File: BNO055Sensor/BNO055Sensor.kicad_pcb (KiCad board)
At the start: 4 copper layers, 50 x 35 mm, 3 parts, among them J1 locked

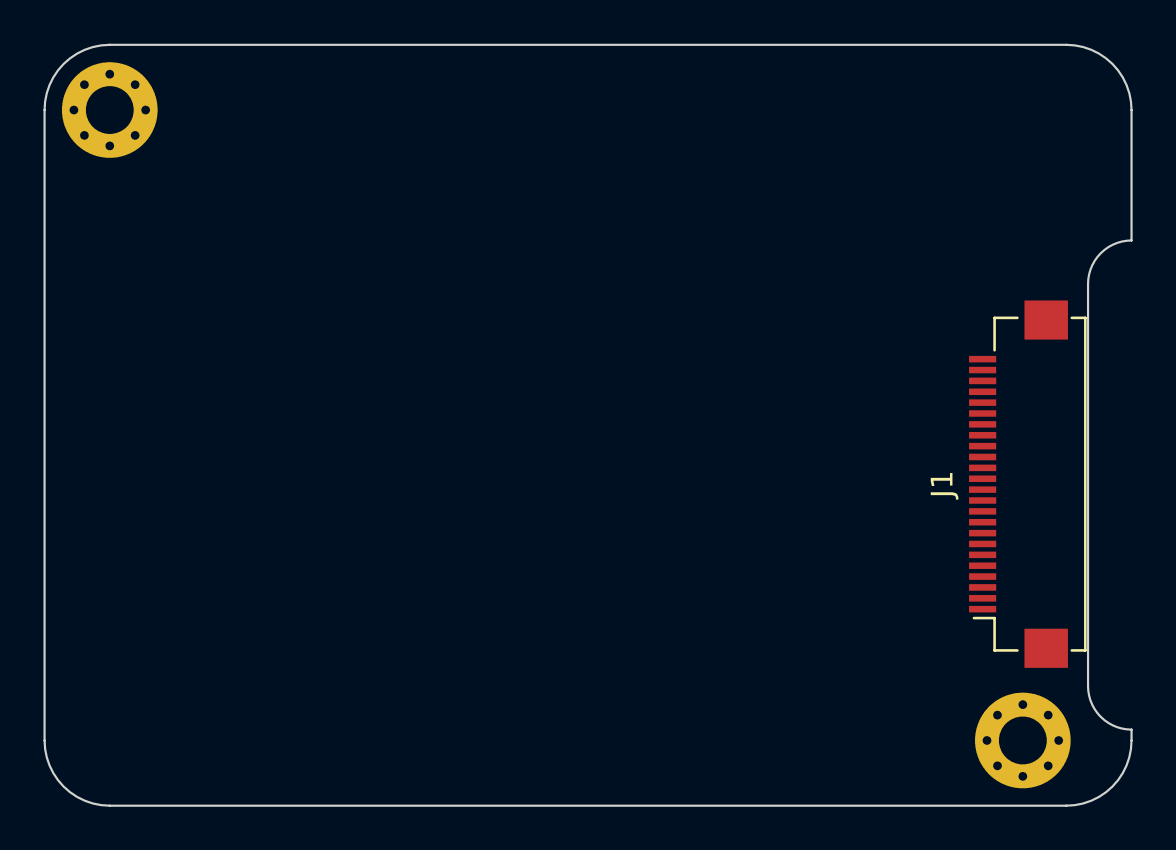
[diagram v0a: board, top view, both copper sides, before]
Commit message: Roughly places components on BNO055 sensor pcb
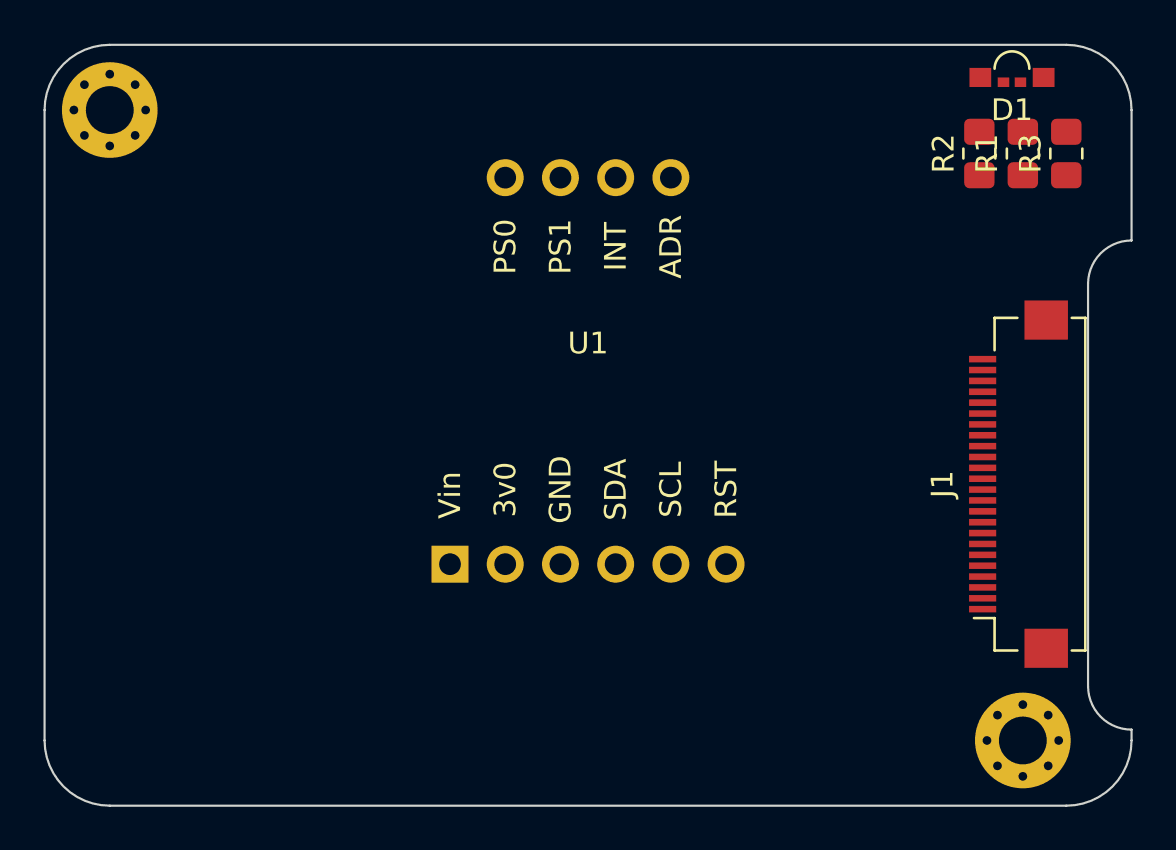
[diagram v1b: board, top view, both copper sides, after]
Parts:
- added D1: LED_RGBA, GameOver:Hongzhi_Forest_HS-1204-RGB, F.Cu at (164.5, 81.5)
- added R1: 1kΩ, Resistor_SMD:R_0805_2012Metric_Pad1.20x1.40mm_HandSolder, F.Cu at (165.0, 85.0)
- added R2: 1kΩ, Resistor_SMD:R_0805_2012Metric_Pad1.20x1.40mm_HandSolder, F.Cu at (163.0, 85.0)
- added R3: 1kΩ, Resistor_SMD:R_0805_2012Metric_Pad1.20x1.40mm_HandSolder, F.Cu at (167.0, 85.0)
- added U1: Adafruit_BNO055_breakout, GameOver:Adafruit_BNO055_breakout, F.Cu at (145.0, 93.7)
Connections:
- net 3v3 renamed +3V3
- H1 pad 1: unconnected-(H1-Pad1) -> GND
- H2 pad 1: unconnected-(H2-Pad1) -> GND
- J1 pad 10: unconnected-(J1-IO5) -> PS0
- J1 pad 11: unconnected-(J1-IO17) -> PS1
- J1 pad 14: unconnected-(J1-IO16) -> INT
- J1 pad 15: unconnected-(J1-IO4) -> ADR
- J1 pad 20: unconnected-(J1-IO35) -> LED_B
- J1 pad 21: unconnected-(J1-IO32) -> LED_G
- J1 pad 22: unconnected-(J1-IO33) -> LED_R
- J1 pad 5: unconnected-(J1-IO21) -> RST
- J1 pad 6: unconnected-(J1-IO19) -> SDA
- J1 pad 9: unconnected-(J1-IO18) -> SCL

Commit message: Adds copper pours for gnd and 3v3 on sensor board
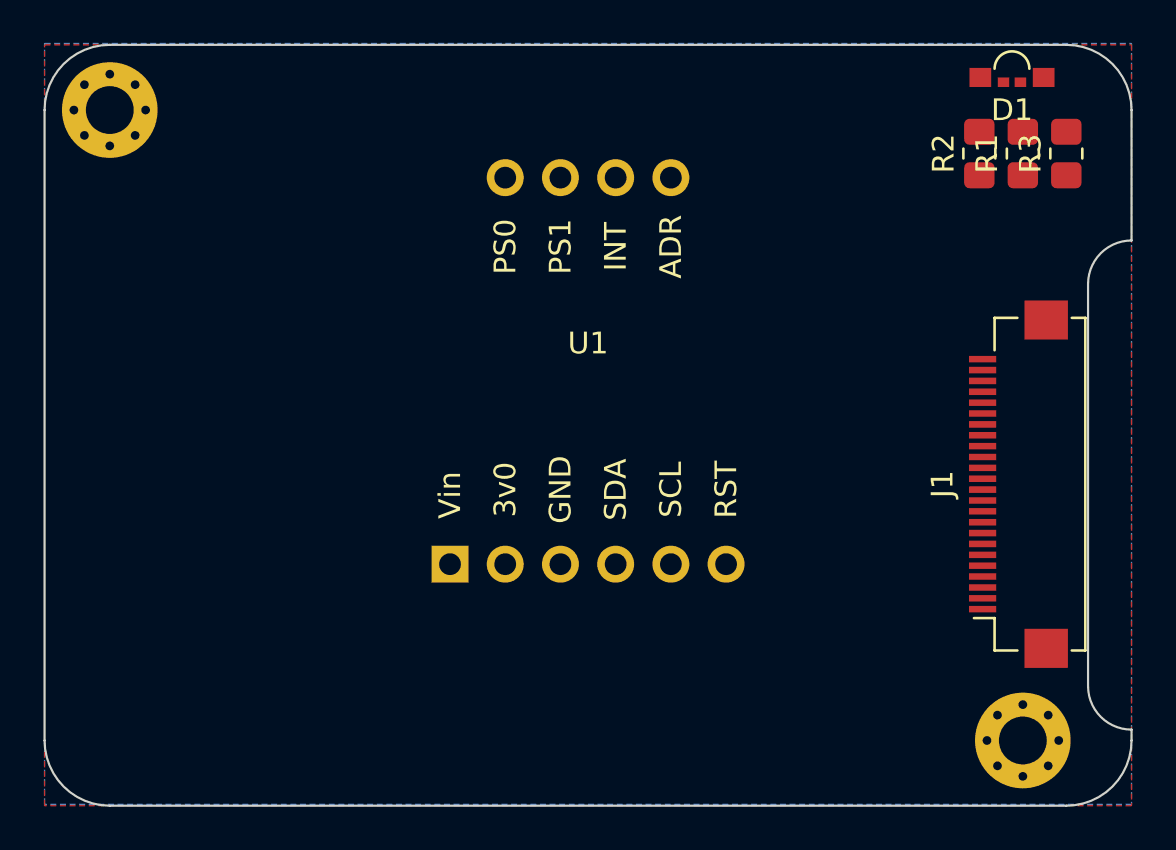
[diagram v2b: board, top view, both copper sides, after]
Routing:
- added copper zone on F.Cu, net +3V3
- added copper zone on B.Cu, net GND
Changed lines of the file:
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@@
   (gr_arc locked (start 167 80) (mid 169.12132 80.87868) (end 170 83)
     (stroke (width 0.1) (type default)) (layer "Edge.Cuts"))
+  (zone (net 7) (net_name "+3V3") (layer "F.Cu") (hatch edge 0.508)
+    (connect_pads (clearance 0.508))
+    (min_thickness 0.254) (filled_areas_thickness no)
+    (fill yes (thermal_gap 0.508) (thermal_bridge_width 0.508) (island_removal_mode 2) (island_area_min 10))
+    (polygon
+      (pts
+        (xy 170 115)
+        (xy 120 115)
+        (xy 120 80)
+        (xy 170 80)
+      )
+    )
+  )
+  (zone (net 1) (net_name "GND") (layer "B.Cu") (hatch edge 0.508)
+    (connect_pads (clearance 0.508))
+    (min_thickness 0.254) (filled_areas_thickness no)
+    (fill yes (thermal_gap 0.508) (thermal_bridge_width 0.508) (island_removal_mode 2) (island_area_min 10))
+    (polygon
+      (pts
+        (xy 170 114.93809)
+        (xy 120 114.93809)
+        (xy 120 79.93809)
+        (xy 170 79.93809)
+      )
+    )
+  )
 )

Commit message: Routes BNO055 breakout board
The SDA/SCL pins shouldn't be swapped as we're using the hardware i2c
which are in set pins on the esp32 (18/19).
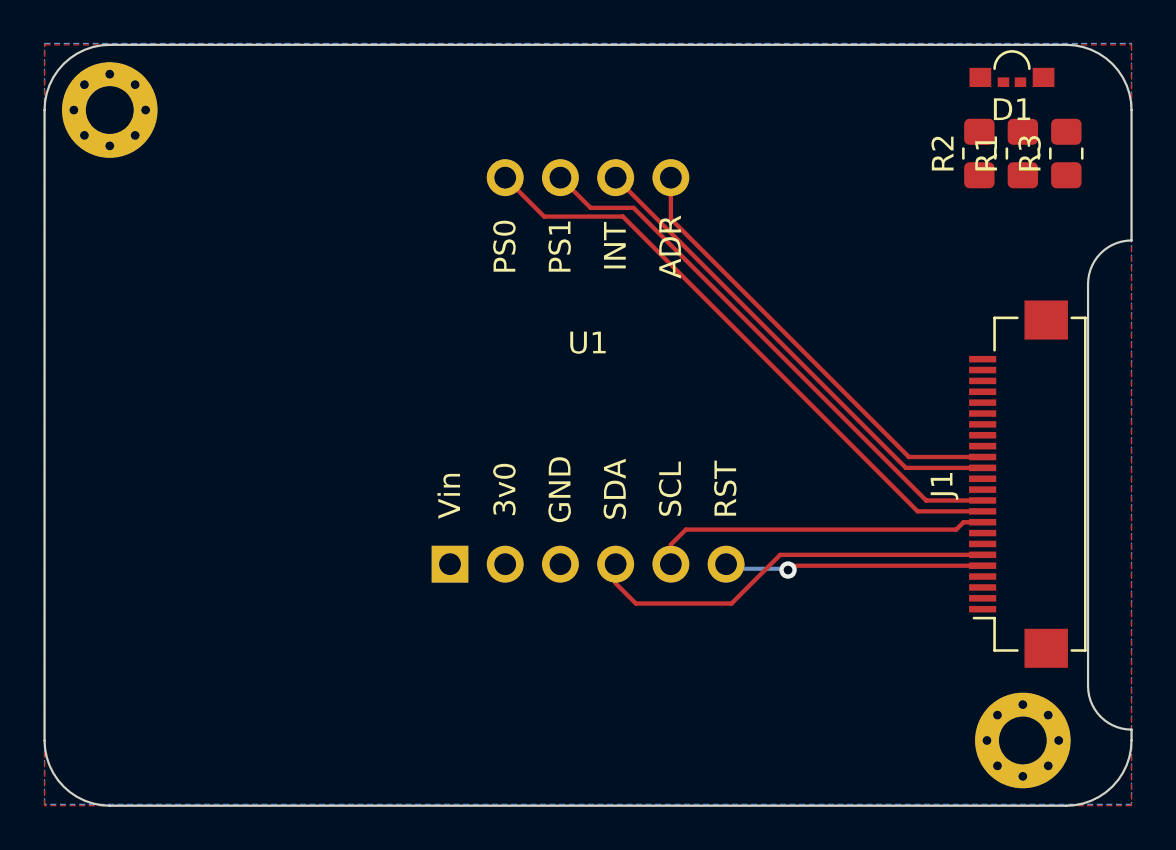
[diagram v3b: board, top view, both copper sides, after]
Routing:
- net PS0: track 0.00 -> 28.3 mm
- net PS1: track 0.00 -> 25.6 mm
- net INT: track 0.00 -> 22.4 mm
- net ADR: track 0.00 -> 20.8 mm
- net SDA: track 0.00 -> 19.1 mm
- net SCL: track 0.00 -> 15.7 mm
- net RST: track 0.00 -> 12.0 mm, vias 0 -> 1
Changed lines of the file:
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@@
   (gr_arc locked (start 167 80) (mid 169.12132 80.87868) (end 170 83)
     (stroke (width 0.1) (type default)) (layer "Edge.Cuts"))
+  (segment (start 154.3995 103.96) (end 163.15 103.96) (width 0.2) (layer "F.Cu") (net 8))
+  (segment (start 154.2 104.1595) (end 154.3995 103.96) (width 0.2) (layer "F.Cu") (net 8))
+  (via (at 154.2 104.1595) (size 0.8) (drill 0.4) (layers "F.Cu" "B.Cu") (net 8))
+  (segment (start 154.1405 104.1) (end 151.56 104.1) (width 0.2) (layer "B.Cu") (net 8))
+  (segment (start 151.56 104.1) (end 151.35 103.89) (width 0.2) (layer "B.Cu") (net 8))
+  (segment (start 154.2 104.1595) (end 154.1405 104.1) (width 0.2) (layer "B.Cu") (net 8))
+  (segment (start 151.6 105.7) (end 147.2 105.7) (width 0.2) (layer "F.Cu") (net 9))
+  (segment (start 153.84 103.46) (end 151.6 105.7) (width 0.2) (layer "F.Cu") (net 9))
+  (segment (start 147.2 105.7) (end 146.27 104.77) (width 0.2) (layer "F.Cu") (net 9))
+  (segment (start 163.15 103.46) (end 153.84 103.46) (width 0.2) (layer "F.Cu") (net 9))
+  (segment (start 146.27 104.77) (end 146.27 103.89) (width 0.2) (layer "F.Cu") (net 9))
+  (segment (start 148.81 102.99) (end 148.81 103.89) (width 0.2) (layer "F.Cu") (net 10))
+  (segment (start 163.15 101.96) (end 162.275978 101.96) (width 0.2) (layer "F.Cu") (net 10))
+  (segment (start 162.275978 101.96) (end 161.935978 102.3) (width 0.2) (layer "F.Cu") (net 10))
+  (segment (start 161.935978 102.3) (end 149.5 102.3) (width 0.2) (layer "F.Cu") (net 10))
+  (segment (start 149.5 102.3) (end 148.81 102.99) (width 0.2) (layer "F.Cu") (net 10))
+  (segment (start 142.98 87.9) (end 141.19 86.11) (width 0.2) (layer "F.Cu") (net 11))
+  (segment (start 160.16 101.46) (end 146.6 87.9) (width 0.2) (layer "F.Cu") (net 11))
+  (segment (start 163.15 101.46) (end 160.16 101.46) (width 0.2) (layer "F.Cu") (net 11))
+  (segment (start 146.6 87.9) (end 142.98 87.9) (width 0.2) (layer "F.Cu") (net 11))
+  (segment (start 163.15 100.96) (end 160.554994 100.96) (width 0.2) (layer "F.Cu") (net 12))
+  (segment (start 160.554994 100.96) (end 147.094994 87.5) (width 0.2) (layer "F.Cu") (net 12))
+  (segment (start 145.12 87.5) (end 143.73 86.11) (width 0.2) (layer "F.Cu") (net 12))
+  (segment (start 147.094994 87.5) (end 145.12 87.5) (width 0.2) (layer "F.Cu") (net 12))
+  (segment (start 159.62 99.46) (end 163.15 99.46) (width 0.2) (layer "F.Cu") (net 13))
+  (segment (start 146.27 86.11) (end 159.62 99.46) (width 0.2) (layer "F.Cu") (net 13))
+  (segment (start 148.81 88.01) (end 148.81 86.11) (width 0.2) (layer "F.Cu") (net 17))
+  (segment (start 159.76 98.96) (end 148.81 88.01) (width 0.2) (layer "F.Cu") (net 17))
+  (segment (start 163.15 98.96) (end 159.76 98.96) (width 0.2) (layer "F.Cu") (net 17))
   (zone (net 7) (net_name "+3V3") (layer "F.Cu") (hatch edge 0.508)
     (connect_pads (clearance 0.508))

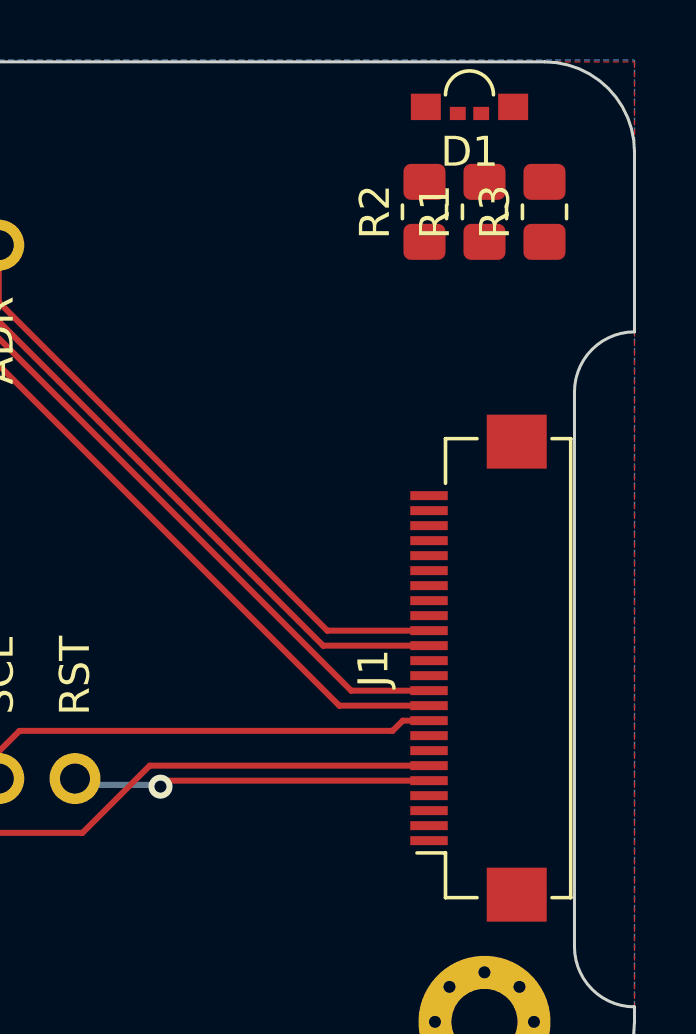
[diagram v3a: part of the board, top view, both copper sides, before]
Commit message: Routes RGB led on sensor board
Some pin reorganization was necessary
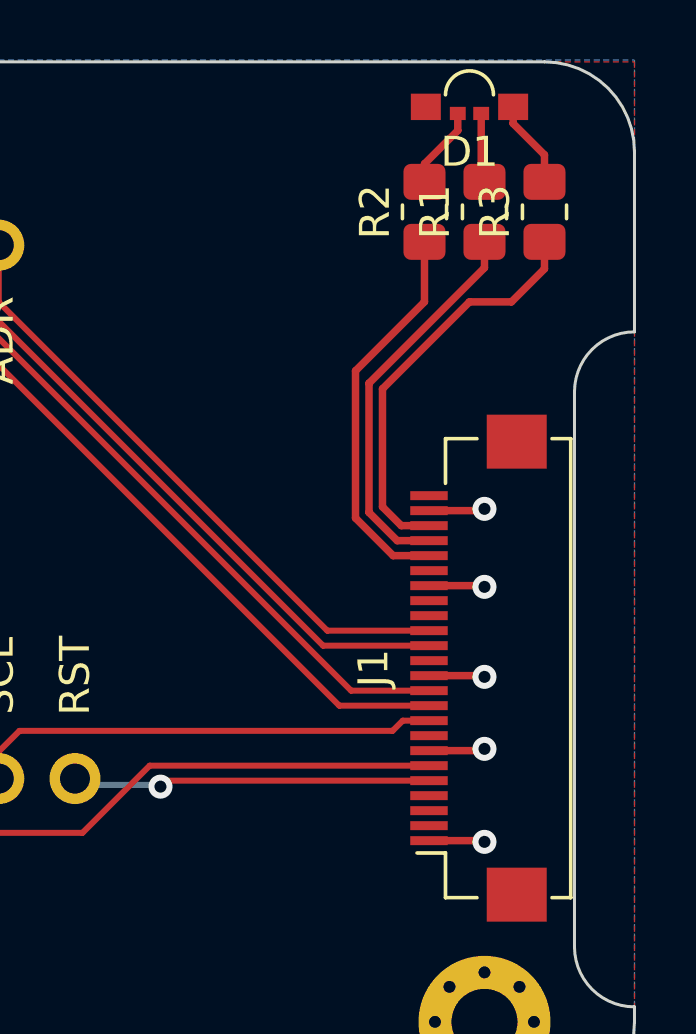
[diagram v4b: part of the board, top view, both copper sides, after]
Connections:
- J1 pad 20: LED_B -> LED_G
- J1 pad 21: LED_G -> LED_R
- J1 pad 22: LED_R -> LED_B
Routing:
- net LED_B: track 0.00 -> 13.7 mm
- net LED_G: track 0.00 -> 13.1 mm
- net LED_R: track 0.00 -> 13.0 mm
- net GND: track 0.00 -> 9.35 mm, vias 0 -> 5
- net Net-(D1-BK): track 0.00 -> 2.93 mm
- net Net-(D1-GK): track 0.00 -> 2.74 mm
- net Net-(D1-RK): track 0.00 -> 2.33 mm
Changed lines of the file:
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@@
       (net 16 "unconnected-(J1-IO34)") (pinfunction "IO34") (pintype "bidirectional+no_connect"))
     (pad "20" smd rect locked (at 3.75 -1.85 90) (size 0.3 1.25) (layers "F.Cu" "F.Paste" "F.Mask")
-      (net 18 "LED_B") (pinfunction "IO35") (pintype "bidirectional"))
+      (net 19 "LED_G") (pinfunction "IO35") (pintype "bidirectional"))
     (pad "21" smd rect locked (at 4.25 -1.85 90) (size 0.3 1.25) (layers "F.Cu" "F.Paste" "F.Mask")
-      (net 19 "LED_G") (pinfunction "IO32") (pintype "bidirectional"))
+      (net 20 "LED_R") (pinfunction "IO32") (pintype "bidirectional"))
     (pad "22" smd rect locked (at 4.75 -1.85 90) (size 0.3 1.25) (layers "F.Cu" "F.Paste" "F.Mask")
-      (net 20 "LED_R") (pinfunction "IO33") (pintype "bidirectional"))
+      (net 18 "LED_B") (pinfunction "IO33") (pintype "bidirectional"))
     (pad "23" smd rect locked (at 5.25 -1.85 90) (size 0.3 1.25) (layers "F.Cu" "F.Paste" "F.Mask")
       (net 1 "GND") (pinfunction "GND") (pintype "power_in"))
@@
   (gr_arc locked (start 167 80) (mid 169.12132 80.87868) (end 170 83)
     (stroke (width 0.1) (type default)) (layer "Edge.Cuts"))
+  (segment (start 163.15 94.96) (end 164.94 94.96) (width 0.25) (layer "F.Cu") (net 1))
+  (segment (start 164.96 105.96) (end 165 106) (width 0.25) (layer "F.Cu") (net 1))
+  (segment (start 163.15 105.96) (end 164.96 105.96) (width 0.25) (layer "F.Cu") (net 1))
+  (segment (start 164.96 100.46) (end 165 100.5) (width 0.25) (layer "F.Cu") (net 1))
+  (segment (start 164.94 94.96) (end 165 94.9) (width 0.25) (layer "F.Cu") (net 1))
+  (segment (start 163.15 100.46) (end 164.96 100.46) (width 0.25) (layer "F.Cu") (net 1))
+  (segment (start 164.94 102.96) (end 165 102.9) (width 0.25) (layer "F.Cu") (net 1))
+  (segment (start 164.96 97.46) (end 165 97.5) (width 0.25) (layer "F.Cu") (net 1))
+  (segment (start 163.15 97.46) (end 164.96 97.46) (width 0.25) (layer "F.Cu") (net 1))
+  (segment (start 163.15 102.96) (end 164.94 102.96) (width 0.25) (layer "F.Cu") (net 1))
+  (via (at 165 94.9) (size 0.8) (drill 0.4) (layers "F.Cu" "B.Cu") (net 1))
+  (via (at 165 102.9) (size 0.8) (drill 0.4) (layers "F.Cu" "B.Cu") (net 1))
+  (via (at 165 106) (size 0.8) (drill 0.4) (layers "F.Cu" "B.Cu") (net 1))
+  (via (at 165 97.5) (size 0.8) (drill 0.4) (layers "F.Cu" "B.Cu") (net 1))
+  (via (at 165 100.5) (size 0.8) (drill 0.4) (layers "F.Cu" "B.Cu") (net 1))
+  (segment (start 164.89 81.72) (end 164.89 83.89) (width 0.25) (layer "F.Cu") (net 2))
+  (segment (start 164.89 83.89) (end 165 84) (width 0.25) (layer "F.Cu") (net 2))
+  (segment (start 163 83.4) (end 164.11 82.29) (width 0.25) (layer "F.Cu") (net 3))
+  (segment (start 164.11 82.29) (end 164.11 81.72) (width 0.25) (layer "F.Cu") (net 3))
+  (segment (start 163 84) (end 163 83.4) (width 0.25) (layer "F.Cu") (net 3))
+  (segment (start 167 83.1) (end 167 84) (width 0.25) (layer "F.Cu") (net 4))
+  (segment (start 165.955 81.5) (end 165.955 82.055) (width 0.25) (layer "F.Cu") (net 4))
+  (segment (start 165.955 82.055) (end 167 83.1) (width 0.25) (layer "F.Cu") (net 4))
   (segment (start 154.3995 103.96) (end 163.15 103.96) (width 0.2) (layer "F.Cu") (net 8))
   (segment (start 154.2 104.1595) (end 154.3995 103.96) (width 0.2) (layer "F.Cu") (net 8))
@@
   (segment (start 159.76 98.96) (end 148.81 88.01) (width 0.2) (layer "F.Cu") (net 17))
   (segment (start 163.15 98.96) (end 159.76 98.96) (width 0.2) (layer "F.Cu") (net 17))
+  (segment (start 165.9 88) (end 167 86.9) (width 0.25) (layer "F.Cu") (net 18))
+  (segment (start 167 86.9) (end 167 86) (width 0.25) (layer "F.Cu") (net 18))
+  (segment (start 163.15 95.46) (end 162.225978 95.46) (width 0.25) (layer "F.Cu") (net 18))
+  (segment (start 161.6 90.9) (end 164.5 88) (width 0.25) (layer "F.Cu") (net 18))
+  (segment (start 164.5 88) (end 165.9 88) (width 0.25) (layer "F.Cu") (net 18))
+  (segment (start 162.225978 95.46) (end 161.6 94.834022) (width 0.25) (layer "F.Cu") (net 18))
+  (segment (start 161.6 94.834022) (end 161.6 90.9) (width 0.25) (layer "F.Cu") (net 18))
+  (segment (start 160.70096 90.29904) (end 163 88) (width 0.25) (layer "F.Cu") (net 19))
+  (segment (start 163.15 96.46) (end 161.954542 96.46) (width 0.25) (layer "F.Cu") (net 19))
+  (segment (start 160.70096 95.206417) (end 160.70096 90.29904) (width 0.25) (layer "F.Cu") (net 19))
+  (segment (start 163 88) (end 163 86) (width 0.25) (layer "F.Cu") (net 19))
+  (segment (start 161.954542 96.46) (end 160.70096 95.206417) (width 0.25) (layer "F.Cu") (net 19))
+  (segment (start 162.09026 95.96) (end 161.15048 95.02022) (width 0.25) (layer "F.Cu") (net 20))
+  (segment (start 161.15048 90.713802) (end 165 86.864282) (width 0.25) (layer "F.Cu") (net 20))
+  (segment (start 161.15048 95.02022) (end 161.15048 90.713802) (width 0.25) (layer "F.Cu") (net 20))
+  (segment (start 163.15 95.96) (end 162.09026 95.96) (width 0.25) (layer "F.Cu") (net 20))
+  (segment (start 165 86.864282) (end 165 86) (width 0.25) (layer "F.Cu") (net 20))
   (zone (net 7) (net_name "+3V3") (layer "F.Cu") (hatch edge 0.508)
     (connect_pads (clearance 0.508))
